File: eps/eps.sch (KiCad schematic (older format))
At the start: 3 parts, among them U4 STM32F411CEUx

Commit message: add analog mux for current sense
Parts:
- removed U4: STM32F411CEUx, Package_DFN_QFN:QFN-48-1EP_7x7mm_P0.5mm_EP5.6x5.6mm, symbol MCU_ST_STM32F4:STM32F411CEUx
- added R?: 100K, symbol Device:R
- added TH1: 100K NTC, symbol Device:Thermistor_NTC
- added U?: STM32F103C8Tx, Package_QFP:LQFP-48_7x7mm_P0.5mm, symbol MCU_ST_STM32F1:STM32F103C8Tx
- added U?: CD74HC4067M, Package_SO:SOIC-24W_7.5x15.4mm_P1.27mm, symbol 74xx:CD74HC4067M
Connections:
- net labels added: 3V3RAW, AMUX1, BRDTMP, I12V, I3V3, I5V, IBATV, IBCR_OUT, ISW1, ISW10, ISW2, ISW3, ISW4, ISW5, ISW6, ISW7, ISW8, ISW9
- wire segments 23 -> 26
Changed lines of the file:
@@
 Regulates solar panel voltage\nReads telemetry from panels\n
 $Comp
-L MCU_ST_STM32F4:STM32F411CEUx U4
-U 1 1 61A79014
-P 8750 2750
-F 0 "U4" H 8700 4431 50  0000 C CNN
-F 1 "STM32F411CEUx" H 8700 4340 50  0000 C CNN
-F 2 "Package_DFN_QFN:QFN-48-1EP_7x7mm_P0.5mm_EP5.6x5.6mm" H 8150 1250 50  0001 R CNN
-F 3 "http://www.st.com/st-web-ui/static/active/en/resource/technical/document/datasheet/DM00115249.pdf" H 8750 2750 50  0001 C CNN
-	1    8750 2750
+L MCU_ST_STM32F1:STM32F103C8Tx U?
+U 1 1 61A4AF8D
+P 9550 2600
+F 0 "U?" H 9500 1011 50  0000 C CNN
+F 1 "STM32F103C8Tx" H 9500 920 50  0000 C CNN
+F 2 "Package_QFP:LQFP-48_7x7mm_P0.5mm" H 8950 1200 50  0001 R CNN
+F 3 "http://www.st.com/st-web-ui/static/active/en/resource/technical/document/datasheet/CD00161566.pdf" H 9550 2600 50  0001 C CNN
+	1    9550 2600
 	1    0    0    -1
 $EndComp
+$Comp
+L 74xx:CD74HC4067M U?
+U 1 1 61A4E99D
+P 6000 1900
+F 0 "U?" H 6000 3081 50  0000 C CNN
+F 1 "CD74HC4067M" H 6000 2990 50  0000 C CNN
+F 2 "Package_SO:SOIC-24W_7.5x15.4mm_P1.27mm" H 6900 900 50  0001 C CIN
+F 3 "http://www.ti.com/lit/ds/symlink/cd74hc4067.pdf" H 5650 2750 50  0001 C CNN
+	1    6000 1900
+	1    0    0    -1
+$EndComp
+Text GLabel 6500 1200 2    50   Input ~ 0
+IBCR_OUT
+Text GLabel 6500 1400 2    50   Input ~ 0
+IBATV
+Text GLabel 6500 1500 2    50   Input ~ 0
+I5V
+Text GLabel 6500 1600 2    50   Input ~ 0
+I3V3
+Text GLabel 6500 1300 2    50   Input ~ 0
+I12V
+Text GLabel 6500 1700 2    50   Input ~ 0
+ISW1
+Text GLabel 6500 1800 2    50   Input ~ 0
+ISW2
+Text GLabel 6500 1900 2    50   Input ~ 0
+ISW3
+Text GLabel 6500 2000 2    50   Input ~ 0
+ISW4
+Text GLabel 6500 2100 2    50   Input ~ 0
+ISW5
+Text GLabel 6500 2200 2    50   Input ~ 0
+ISW6
+Text GLabel 6500 2300 2    50   Input ~ 0
+ISW7
+Text GLabel 6500 2400 2    50   Input ~ 0
+ISW8
+Text GLabel 6500 2500 2    50   Input ~ 0
+ISW9
+Text GLabel 6500 2600 2    50   Input ~ 0
+ISW10
+$Comp
+L Device:R R?
+U 1 1 61A6406C
+P 7750 2200
+F 0 "R?" H 7820 2246 50  0000 L CNN
+F 1 "100K" H 7820 2155 50  0000 L CNN
+F 2 "" V 7680 2200 50  0001 C CNN
+F 3 "~" H 7750 2200 50  0001 C CNN
+	1    7750 2200
+	1    0    0    -1
+$EndComp
+Wire Wire Line
+	7750 2050 7750 2000
+Text GLabel 7750 1700 1    50   Input ~ 0
+3V3RAW
+$Comp
+L power:GND #PWR?
+U 1 1 61A65B64
+P 7750 2350
+F 0 "#PWR?" H 7750 2100 50  0001 C CNN
+F 1 "GND" H 7755 2177 50  0000 C CNN
+F 2 "" H 7750 2350 50  0001 C CNN
+F 3 "" H 7750 2350 50  0001 C CNN
+	1    7750 2350
+	1    0    0    -1
+$EndComp
+$Comp
+L Device:Thermistor_NTC TH1
+U 1 1 61A667A8
+P 7750 1850
+F 0 "TH1" H 7848 1896 50  0000 L CNN
+F 1 "100K NTC" H 7848 1805 50  0000 L CNN
+F 2 "" H 7750 1900 50  0001 C CNN
+F 3 "~" H 7750 1900 50  0001 C CNN
+	1    7750 1850
+	1    0    0    -1
+$EndComp
+Wire Wire Line
+	7750 2000 7550 2000
+Connection ~ 7750 2000
+Text Label 7550 2000 2    50   ~ 0
+BRDTMP
+Text Label 6500 2700 0    50   ~ 0
+BRDTMP
+Text GLabel 5650 900  0    50   Input ~ 0
+3V3RAW
+Wire Wire Line
+	6000 900  5650 900
+$Comp
+L power:GND #PWR?
+U 1 1 61A6DD8E
+P 6000 3000
+F 0 "#PWR?" H 6000 2750 50  0001 C CNN
+F 1 "GND" H 6005 2827 50  0000 C CNN
+F 2 "" H 6000 3000 50  0001 C CNN
+F 3 "" H 6000 3000 50  0001 C CNN
+	1    6000 3000
+	1    0    0    -1
+$EndComp
+Text Label 5500 1400 2    50   ~ 0
+AMUX1
 $EndSCHEMATC

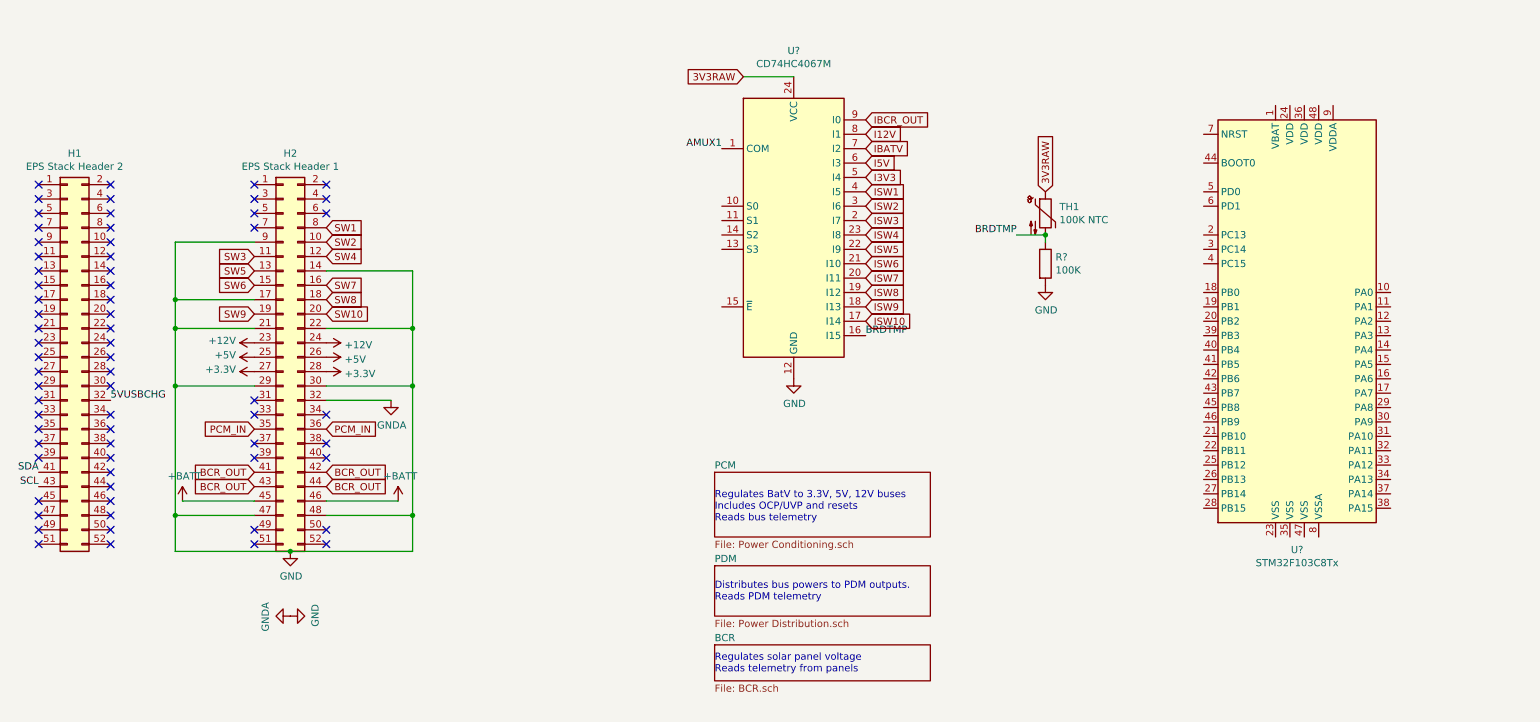
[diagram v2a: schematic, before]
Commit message: add watchdog ic and mppt ics
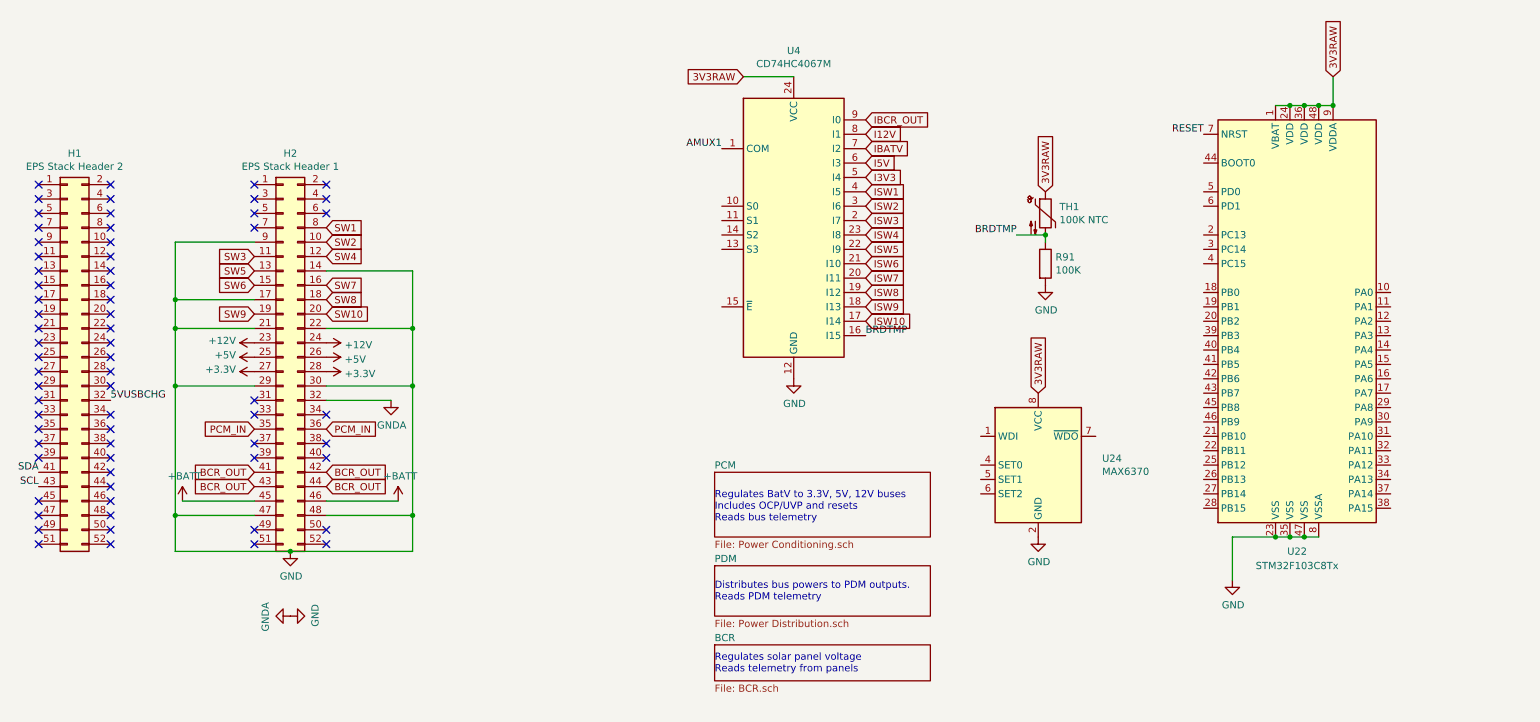
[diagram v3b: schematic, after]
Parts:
- added U24: MAX6370, Package_TO_SOT_SMD:SOT-23-8, symbol Power_Supervisor:MAX6370
- gave numbers to parts that had none: 3
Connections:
- net 3V3RAW: now also U22.1 (VBAT), U22.24 (VDD), U22.36 (VDD), U22.48 (VDD), U22.9 (VDDA), U24.8 (VCC)
- net GND: now also U22.23 (VSS), U22.35 (VSS), U22.47 (VSS), U22.8 (VSSA), U24.2 (GND)
- net RESET: now reaches U22.7 (NRST)
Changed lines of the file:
@@
 Regulates solar panel voltage\nReads telemetry from panels\n
 $Comp
-L MCU_ST_STM32F1:STM32F103C8Tx U?
+L MCU_ST_STM32F1:STM32F103C8Tx U22
 U 1 1 61A4AF8D
 P 9550 2600
-F 0 "U?" H 9500 1011 50  0000 C CNN
-F 1 "STM32F103C8Tx" H 9500 920 50  0000 C CNN
+F 0 "U22" H 9500 1000 50  0000 C CNN
+F 1 "STM32F103C8Tx" H 9500 900 50  0000 C CNN
 F 2 "Package_QFP:LQFP-48_7x7mm_P0.5mm" H 8950 1200 50  0001 R CNN
 F 3 "http://www.st.com/st-web-ui/static/active/en/resource/technical/document/datasheet/CD00161566.pdf" H 9550 2600 50  0001 C CNN
@@
 $EndComp
 $Comp
-L 74xx:CD74HC4067M U?
+L 74xx:CD74HC4067M U4
 U 1 1 61A4E99D
 P 6000 1900
-F 0 "U?" H 6000 3081 50  0000 C CNN
+F 0 "U4" H 6000 3081 50  0000 C CNN
 F 1 "CD74HC4067M" H 6000 2990 50  0000 C CNN
 F 2 "Package_SO:SOIC-24W_7.5x15.4mm_P1.27mm" H 6900 900 50  0001 C CIN
@@
 ISW10
 $Comp
-L Device:R R?
+L Device:R R91
 U 1 1 61A6406C
 P 7750 2200
-F 0 "R?" H 7820 2246 50  0000 L CNN
+F 0 "R91" H 7820 2246 50  0000 L CNN
 F 1 "100K" H 7820 2155 50  0000 L CNN
 F 2 "" V 7680 2200 50  0001 C CNN
@@
 3V3RAW
 $Comp
-L power:GND #PWR?
+L power:GND #PWR053
 U 1 1 61A65B64
 P 7750 2350
-F 0 "#PWR?" H 7750 2100 50  0001 C CNN
+F 0 "#PWR053" H 7750 2100 50  0001 C CNN
 F 1 "GND" H 7755 2177 50  0000 C CNN
 F 2 "" H 7750 2350 50  0001 C CNN
@@
 	6000 900  5650 900
 $Comp
-L power:GND #PWR?
+L power:GND #PWR052
 U 1 1 61A6DD8E
 P 6000 3000
-F 0 "#PWR?" H 6000 2750 50  0001 C CNN
+F 0 "#PWR052" H 6000 2750 50  0001 C CNN
 F 1 "GND" H 6005 2827 50  0000 C CNN
 F 2 "" H 6000 3000 50  0001 C CNN
@@
 Text Label 5500 1400 2    50   ~ 0
 AMUX1
+Wire Wire Line
+	9350 1100 9450 1100
+Wire Wire Line
+	9750 1100 9750 900
+Connection ~ 9750 1100
+Connection ~ 9450 1100
+Wire Wire Line
+	9450 1100 9550 1100
+Connection ~ 9550 1100
+Wire Wire Line
+	9550 1100 9650 1100
+Connection ~ 9650 1100
+Wire Wire Line
+	9650 1100 9750 1100
+Text GLabel 9750 900  1    50   Input ~ 0
+3V3RAW
+Wire Wire Line
+	9650 4100 9550 4100
+Wire Wire Line
+	9050 4100 9050 4400
+Connection ~ 9350 4100
+Wire Wire Line
+	9350 4100 9050 4100
+Connection ~ 9450 4100
+Wire Wire Line
+	9450 4100 9350 4100
+Connection ~ 9550 4100
+Wire Wire Line
+	9550 4100 9450 4100
+$Comp
+L power:GND #PWR054
+U 1 1 618365FA
+P 9050 4400
+F 0 "#PWR054" H 9050 4150 50  0001 C CNN
+F 1 "GND" H 9055 4227 50  0000 C CNN
+F 2 "" H 9050 4400 50  0001 C CNN
+F 3 "" H 9050 4400 50  0001 C CNN
+	1    9050 4400
+	1    0    0    -1
+$EndComp
+Text Label 8850 1300 2    50   ~ 0
+RESET
+$Comp
+L Power_Supervisor:MAX6370 U24
+U 1 1 6183955A
+P 7700 3600
+F 0 "U24" H 8144 3646 50  0000 L CNN
+F 1 "MAX6370" H 8144 3555 50  0000 L CNN
+F 2 "Package_TO_SOT_SMD:SOT-23-8" H 8350 3150 50  0001 C CNN
+F 3 "https://datasheets.maximintegrated.com/en/ds/MAX6369-MAX6374.pdf" H 7850 4100 50  0001 C CNN
+	1    7700 3600
+	1    0    0    -1
+$EndComp
+Text GLabel 7700 3100 1    50   Input ~ 0
+3V3RAW
+$Comp
+L power:GND #PWR055
+U 1 1 6183BB41
+P 7700 4100
+F 0 "#PWR055" H 7700 3850 50  0001 C CNN
+F 1 "GND" H 7705 3927 50  0000 C CNN
+F 2 "" H 7700 4100 50  0001 C CNN
+F 3 "" H 7700 4100 50  0001 C CNN
+	1    7700 4100
+	1    0    0    -1
+$EndComp
 $EndSCHEMATC

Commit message: modify mux, implement hw watchdog, standardize p channel mosfets to irf7425
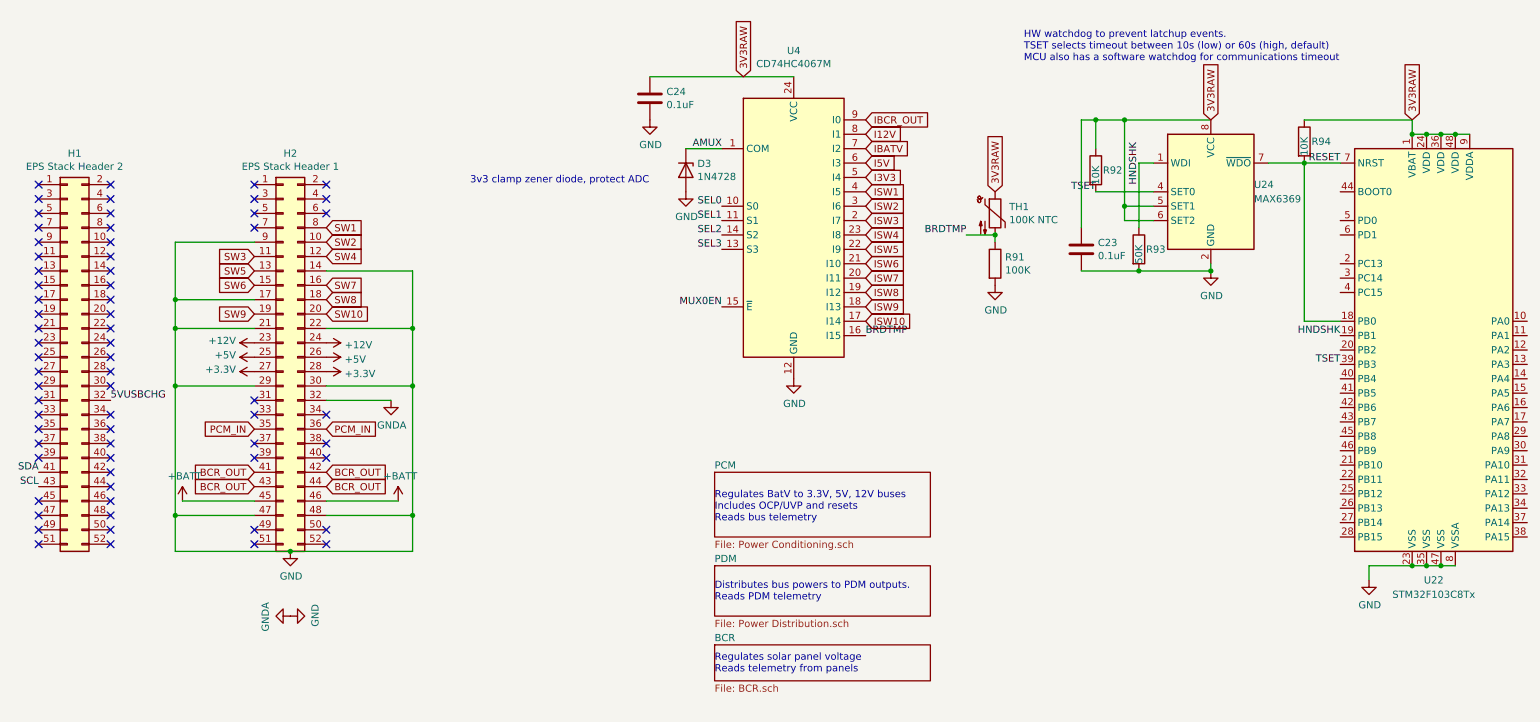
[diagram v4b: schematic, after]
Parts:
- removed U24: MAX6370, Package_TO_SOT_SMD:SOT-23-8, symbol Power_Supervisor:MAX6370
- added C23, C24: 0.1uF, symbol Device:C
- added D3: 1N4728, symbol Device:D_Zener
- added R92, R94: 10K, symbol Device:R
- added R93: 50K, symbol Device:R
- added U24: MAX6369, Package_TO_SOT_SMD:SOT-23-8, symbol Power_Supervisor:MAX6369
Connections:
- net 3V3RAW: now also C23.1, C24.1, R92.1, R94.1, U24.5 (SET1), U24.6 (SET2), U24.8 (VCC)
- net GND: now also C23.2, C24.2, D3.2 (A), R93.2, U24.2 (GND)
- net RESET: now also U22.18 (PB0), R94.2, U24.7 (~WDO)
- net HNDSHK: now reaches U22.19 (PB1)
- net HNDSHK: now also R93.1, U24.1 (WDI)
- net TSET: now reaches U22.39 (PB3)
- net TSET: now also R92.2, U24.4 (SET0)
- net SEL0: now reaches U4.10 (S0)
- net SEL1: now reaches U4.11 (S1)
- net SEL3: now reaches U4.13 (S3)
- net SEL2: now reaches U4.14 (S2)
- net MUX0EN: now reaches U4.15 (~E)
- net AMUX1 renamed AMUX
- net AMUX: now also D3.1 (K)
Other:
- note added: "3v3 clamp zener diode, protect ADC"
- note added: "HW watchdog to prevent latchup events.\nTSET selects timeout between 10s (low) or 60s (high, default)\nMCU also has a software watchdog for communications timeout\n"
- moved on the sheet: R91, TH1, U22

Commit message: voltage dividers and move analog telem to new sheet
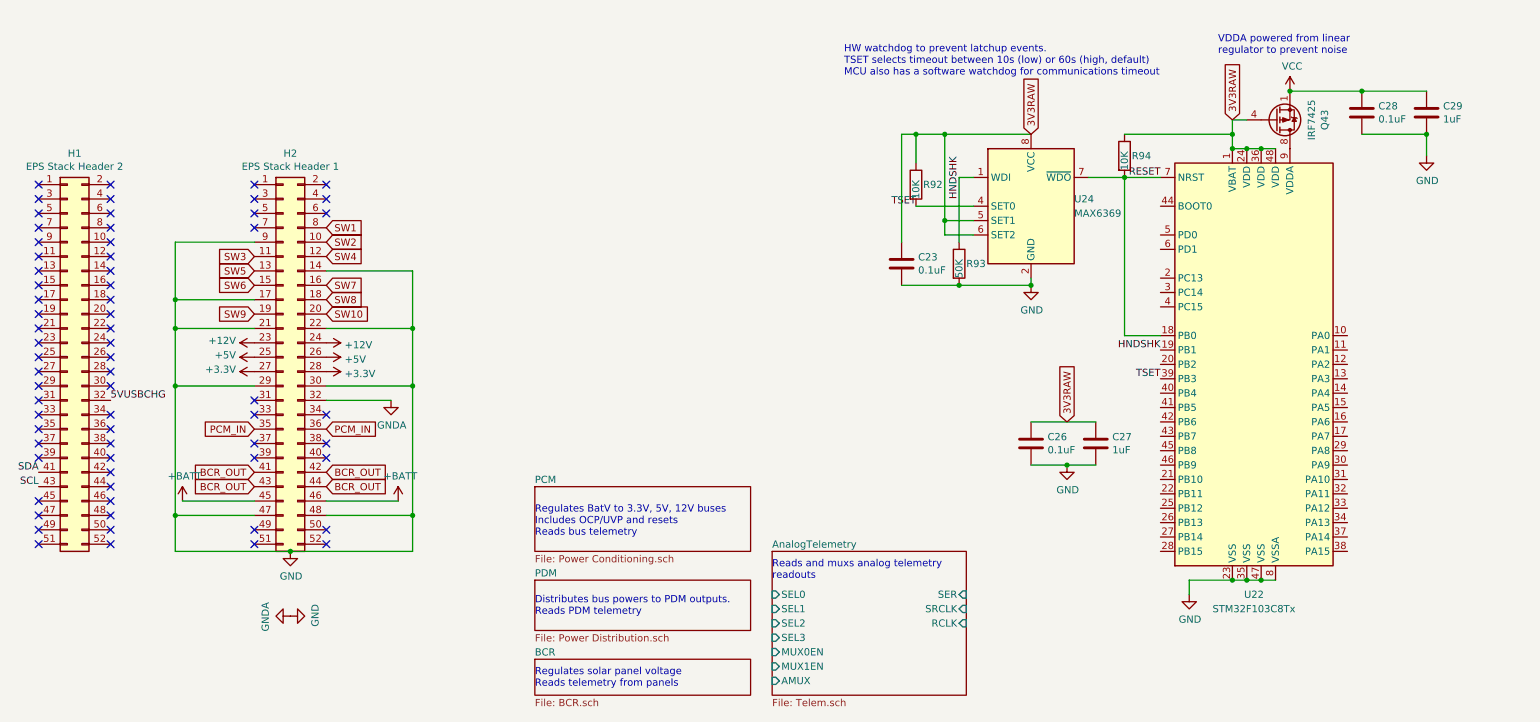
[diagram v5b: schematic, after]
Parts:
- removed C24: 0.1uF, symbol Device:C
- removed D3: 1N4728, symbol Device:D_Zener
- removed R91: 100K, symbol Device:R
- removed TH1: 100K NTC, symbol Device:Thermistor_NTC
- removed U4: CD74HC4067M, Package_SO:SOIC-24W_7.5x15.4mm_P1.27mm, symbol 74xx:CD74HC4067M
- added C26, C28: 0.1uF, symbol Device:C
- added C27, C29: 1uF, symbol Device:C
- added Q43: IRF7425, Package_SO:SOIC-8_3.9x4.9mm_P1.27mm, symbol Transistor_FET:IRF7404
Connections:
- net 3V3RAW: now also C26.1, C27.1, Q43.4 (G); no longer U22.9 (VDDA)
- net GND: now also C26.2, C27.2, C28.2, C29.2
- new net: Q43.5 (D), Q43.6 (D), Q43.7 (D), Q43.8 (D), U22.9 (VDDA)
- new net VCC: C28.1, C29.1, Q43.1 (S), Q43.2 (S), Q43.3 (S)
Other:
- note added: "Reads and muxs analog telemetry\nreadouts"
- note added: "VDDA powered from linear \nregulator to prevent noise"
- note removed: "3v3 clamp zener diode, protect ADC"
- moved on the sheet: C23, R92, R93, R94, U22, U24

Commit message: bcr work
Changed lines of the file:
@@
 $Descr A4 11693 8268
 encoding utf-8
-Sheet 1 8
+Sheet 1 11
 Title "Stopgap EPS for TJREVERB"
 Date "2021-10-22"
@@
 Wire Wire Line
 	3350 3050 3350 3950
-$Comp
-L power:GNDA #PWR010
-U 1 1 61818B53
-P 3200 3150
-F 0 "#PWR010" H 3200 2900 50  0001 C CNN
-F 1 "GNDA" H 3205 2977 50  0000 C CNN
-F 2 "" H 3200 3150 50  0001 C CNN
-F 3 "" H 3200 3150 50  0001 C CNN
-	1    3200 3150
-	1    0    0    -1
-$EndComp
 Wire Wire Line
 	2750 3150 3200 3150
@@
 L power:GNDA #PWR05
 U 1 1 6189C554
-P 2500 4650
-F 0 "#PWR05" H 2500 4400 50  0001 C CNN
-F 1 "GNDA" H 2505 4477 50  0000 C CNN
-F 2 "" H 2500 4650 50  0001 C CNN
-F 3 "" H 2500 4650 50  0001 C CNN
-	1    2500 4650
-	0    1    1    0
+P 2100 4600
+F 0 "#PWR05" H 2100 4350 50  0001 C CNN
+F 1 "GNDA" H 2105 4427 50  0000 C CNN
+F 2 "" H 2100 4600 50  0001 C CNN
+F 3 "" H 2100 4600 50  0001 C CNN
+	1    2100 4600
+	1    0    0    -1
 $EndComp
 $Comp
 L power:GND #PWR06
 U 1 1 618A02B1
-P 2500 4650
-F 0 "#PWR06" H 2500 4400 50  0001 C CNN
-F 1 "GND" H 2505 4477 50  0000 C CNN
-F 2 "" H 2500 4650 50  0001 C CNN
-F 3 "" H 2500 4650 50  0001 C CNN
-	1    2500 4650
-	0    -1   -1   0
+P 2350 4600
+F 0 "#PWR06" H 2350 4350 50  0001 C CNN
+F 1 "GND" H 2355 4427 50  0000 C CNN
+F 2 "" H 2350 4600 50  0001 C CNN
+F 3 "" H 2350 4600 50  0001 C CNN
+	1    2350 4600
+	1    0    0    -1
 $EndComp
 $Sheet
@@
 Text GLabel 9050 1200 1    50   Input ~ 0
 3V3RAW
-Wire Wire Line
-	9350 4400 9250 4400
 Connection ~ 9050 4400
 Wire Wire Line
@@
 Wire Wire Line
 	9150 4400 9050 4400
-Connection ~ 9250 4400
 Wire Wire Line
 	9250 4400 9150 4400
@@
 	10400 1300 10400 1450
 Connection ~ 10400 1300
-$Comp
-L power:GND #PWR081
-U 1 1 61956015
-P 10400 1450
-F 0 "#PWR081" H 10400 1200 50  0001 C CNN
-F 1 "GND" H 10405 1277 50  0000 C CNN
-F 2 "" H 10400 1450 50  0001 C CNN
-F 3 "" H 10400 1450 50  0001 C CNN
-	1    10400 1450
-	1    0    0    -1
-$EndComp
 Text GLabel 7900 3300 1    50   Input ~ 0
 3V3RAW
@@
 Text Notes 5850 4400 0    50   ~ 0
 Reads and muxs analog telemetry\nreadouts
+$Comp
+L power:GNDPWR #PWR?
+U 1 1 6186CCED
+P 3200 3150
+F 0 "#PWR?" H 3200 2950 50  0001 C CNN
+F 1 "GNDPWR" H 3204 2996 50  0000 C CNN
+F 2 "" H 3200 3100 50  0001 C CNN
+F 3 "" H 3200 3100 50  0001 C CNN
+	1    3200 3150
+	1    0    0    -1
+$EndComp
+$Comp
+L power:GNDPWR #PWR?
+U 1 1 6186D9D3
+P 1800 4600
+F 0 "#PWR?" H 1800 4400 50  0001 C CNN
+F 1 "GNDPWR" H 1804 4446 50  0000 C CNN
+F 2 "" H 1800 4550 50  0001 C CNN
+F 3 "" H 1800 4550 50  0001 C CNN
+	1    1800 4600
+	1    0    0    -1
+$EndComp
+Wire Wire Line
+	1800 4600 2100 4600
+Connection ~ 2100 4600
+Wire Wire Line
+	2100 4600 2350 4600
+$Comp
+L power:GNDA #PWR?
+U 1 1 618739A3
+P 9350 4400
+F 0 "#PWR?" H 9350 4150 50  0001 C CNN
+F 1 "GNDA" H 9355 4227 50  0000 C CNN
+F 2 "" H 9350 4400 50  0001 C CNN
+F 3 "" H 9350 4400 50  0001 C CNN
+	1    9350 4400
+	1    0    0    -1
+$EndComp
+$Comp
+L power:GNDA #PWR?
+U 1 1 61877721
+P 10400 1450
+F 0 "#PWR?" H 10400 1200 50  0001 C CNN
+F 1 "GNDA" H 10405 1277 50  0000 C CNN
+F 2 "" H 10400 1450 50  0001 C CNN
+F 3 "" H 10400 1450 50  0001 C CNN
+	1    10400 1450
+	1    0    0    -1
+$EndComp
 $EndSCHEMATC
